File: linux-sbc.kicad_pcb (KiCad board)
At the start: 8 copper layers, 548 parts, among them J1001 7499010121A, J101 Mini-fit Jr 5569, J1101 DM3AT-SF-PEJM5, J1201 PH1-08-UA, J1202 EMI shield frame, J1203 FH12A-40S-0.5SH(55), J1301 SMA RF2-04, J201 61300211121, J202 61300211121, J203 61300211121, J204 61300211121, J205 61300211121, J206 61300211121, J207 61300211121, J208 61300211121, J301 61300211121, J302 61300211121, J303 EMI shield frame, J401 EMI shield frame, J701 USB4105-GF-A, J702 TC2050-NL, J901 AU-Y1008-2-BLK, J902 AU-Y1008-2-BLK, Q201 DMPH4029LFGQ, Q202 DMPH4029LFGQ, Q203 DMN65D8L, Q204 DMPH4029LFGQ, Q205 DMPH4029LFGQ, SW501 JS202011CQN, U1001 LAN8742A-CZ-TR, U1201 TCA9554PW, U1202 AP5725FDCG-7, U1301 LBEE5KL1YN-814, U201 LM4040-5.0, U202 TL331, U203 OPA197, U204 LM4040-5.0, U205 TL331, U206 LM4040-5.0, U207 TL331, U301 AP64500SP-13, U302 AP64500SP-13, U401 STPMIC1DPQR, U501 STM32MP135FAE7, U701 FT231XQ-R, U702 TCA9554PW, U801 MT41K256M16TW, U901 USB2514B/M2, U902 AP22966DC8-7, U903 AP22966DC8-7, Y501 32.768 kHz, Y502 24 MHz, Y901 24 MHz

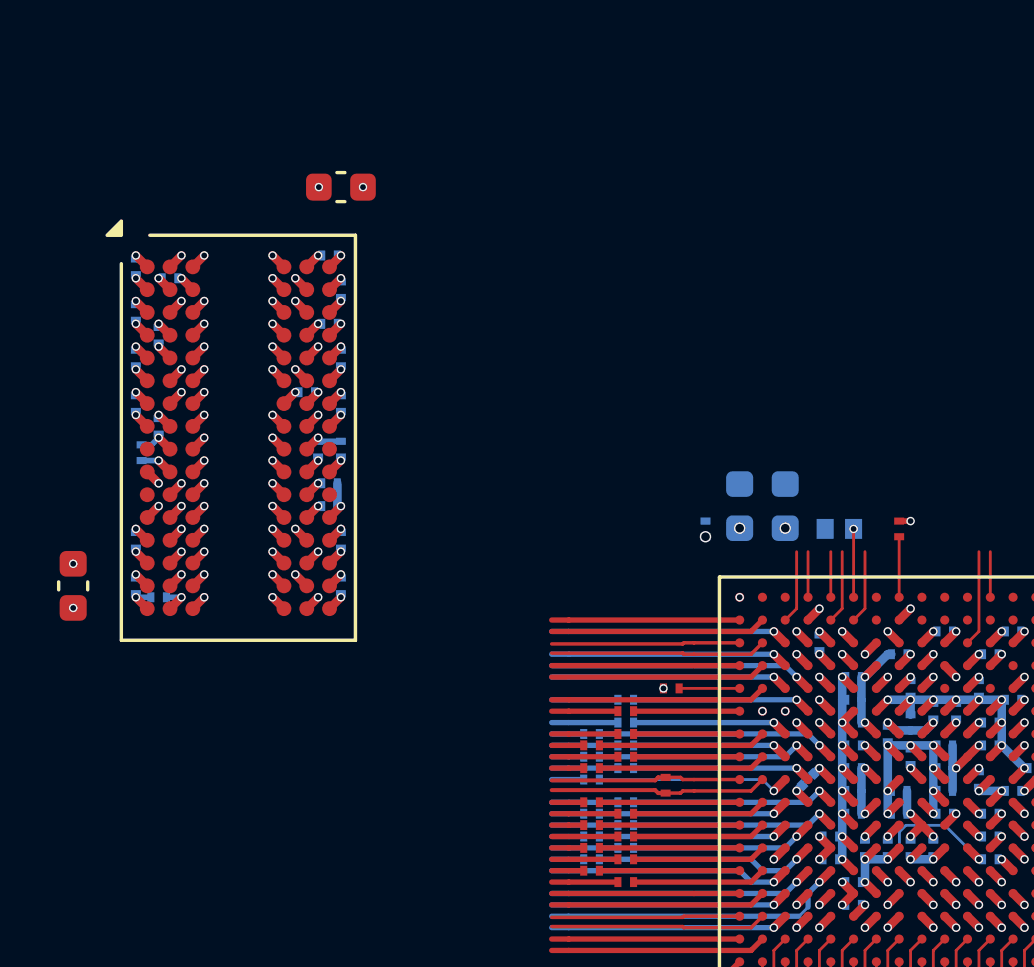
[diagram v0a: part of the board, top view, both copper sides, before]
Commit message: Start layout for DDR power
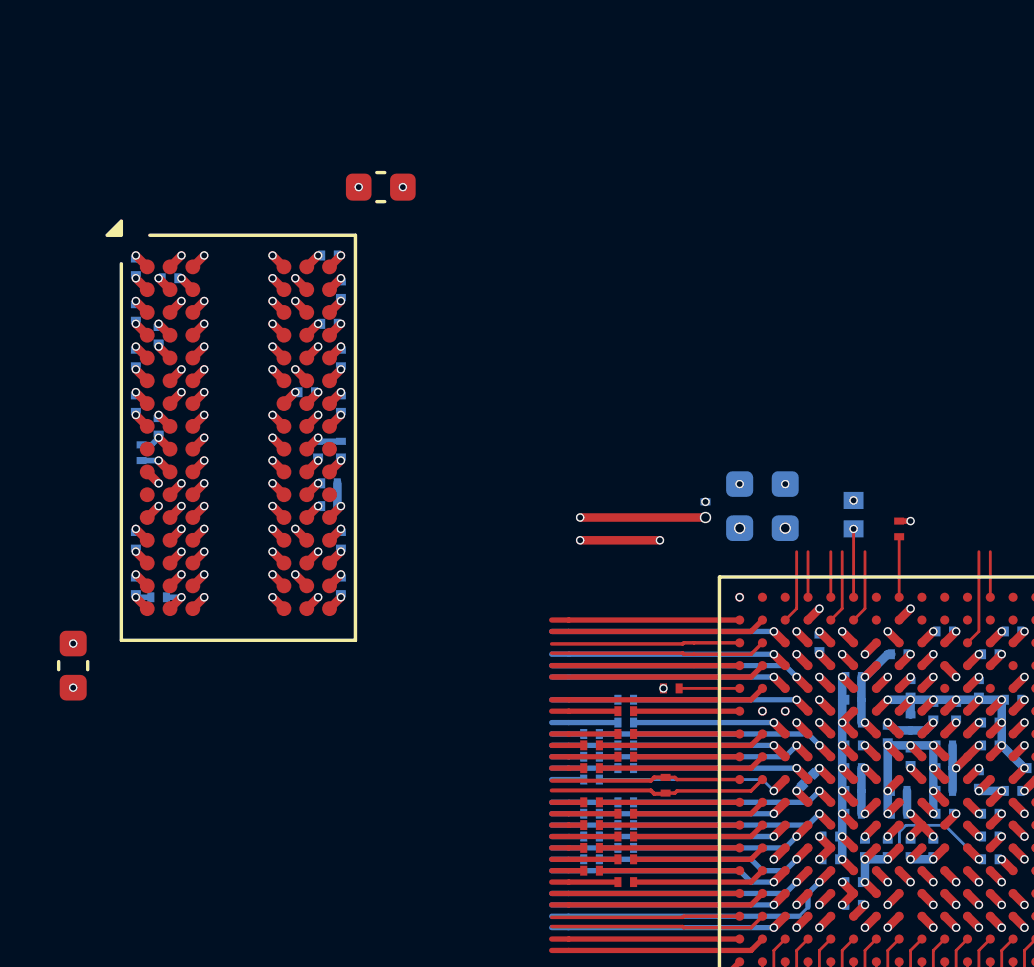
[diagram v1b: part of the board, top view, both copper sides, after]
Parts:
- moved C802 2.80 mm to (-329.8, 96.0)
- moved C801 1.40 mm to (-319.0, 79.2)
- moved R502 0.71 mm to (-302.4, 90.7), turned to 90 degrees
- moved C501 0.67 mm to (-307.6, 90.5)
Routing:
- net /DDR/VDD_DDR: track 32.2 -> 56.2 mm, vias 32 -> 34
- net /DDR/VREF_DDR: track 16.0 -> 39.2 mm, vias 5 -> 6
- net /MPU/VDD_SD_IO: track 27.4 -> 29.8 mm
- net /MPU/VDD_CPU: track 46.7 -> 48.6 mm
- net /MPU/VDD_CORE: track 37.4 -> 39.0 mm
- net GND: vias 243 -> 247
- added copper zone on In2.Cu, net /DDR/VDD_DDR

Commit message: Layout the ethernet section
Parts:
- C1002, C1007, C1008, R1025, R1026: moved to B.Cu
- moved C1007 309.7 mm to (-103.2, -197.0), turned to 90 degrees
- moved C1008 306.1 mm to (-99.6, -191.5), turned to 180 degrees
- moved R1026 301.0 mm to (-96.6, -189.7)
- moved R1025 299.2 mm to (-102.9, -190.2), turned to -90 degrees
- moved R1024 298.7 mm to (-98.0, -184.5), turned to 180 degrees
- moved D1001 298.2 mm to (-100.0, -185.8), turned to 90 degrees
- moved R1023 297.0 mm to (-99.5, -184.5)
- moved R1022 294.7 mm to (-100.5, -183.9), turned to 180 degrees
- moved R1020 291.4 mm to (-102.0, -183.9)
- moved C1006 289.3 mm to (-101.9, -178.0), turned to 180 degrees
- moved R1017 288.8 mm to (-100.5, -173.0)
- moved C1005 288.8 mm to (-96.8, -178.6)
- moved FB1001 288.3 mm to (-96.4, -181.3), turned to 180 degrees
- moved R1021 288.2 mm to (-101.2, -179.0), turned to 180 degrees
- moved R1016 286.0 mm to (-98.5, -171.6)
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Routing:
- net /Ethernet/V_DDA: track 0.00 -> 36.1 mm, vias 0 -> 7
- net CHASSIS: track 0.00 -> 31.7 mm, vias 0 -> 1
- net /Ethernet/LED1_A: track 0.00 -> 26.8 mm, vias 0 -> 2
- net /Ethernet/RX_N: track 0.00 -> 22.1 mm
- net /Ethernet/RX_P: track 0.00 -> 22.1 mm
- net /Ethernet/TX_N: track 0.00 -> 19.0 mm, vias 0 -> 2
- net /Ethernet/TX_P: track 0.00 -> 18.9 mm, vias 0 -> 2
- net /Ethernet/LED2_K: track 0.00 -> 14.2 mm
- net /Ethernet/TXD1: track 0.00 -> 11.1 mm
- net /Ethernet/TXD0: track 0.00 -> 10.0 mm
- net /Ethernet/TXEN: track 0.00 -> 8.80 mm
- net /Ethernet/RST_N: track 0.00 -> 7.32 mm
- net /Ethernet/CLKIN: track 0.00 -> 6.72 mm
- net /Ethernet/MDC: track 0.00 -> 5.24 mm
- net /Ethernet/INT_N: track 0.00 -> 4.38 mm
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- added copper zone on F.Cu, net /Ethernet/V_DDA
- added copper zone on F.Cu, net /Ethernet/V_DDCR

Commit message: Layout the SD card section
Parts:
- C1101: moved to B.Cu
- moved J1101 278.9 mm to (-68.0, -196.0), turned to 180 degrees
- moved C1101 268.3 mm to (-70.2, -183.5), turned to 180 degrees
- moved D1101 264.9 mm to (-68.0, -184.0), turned to -90 degrees
- moved R1109 258.2 mm to (-66.9, -181.0)
- moved R1107 256.5 mm to (-70.0, -182.5)
- moved R1108 255.9 mm to (-66.9, -180.3), turned to 180 degrees
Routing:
- net CHASSIS: track 31.7 -> 75.0 mm, vias 1 -> 6
- net /MPU/uSD.DET_N: track 0.57 -> 31.0 mm, vias 1 -> 4
- net /SD card/D1: track 0.00 -> 11.0 mm
- net /SD card/D2: track 0.00 -> 9.39 mm
- net /PMIC/VDD_SD: track 8.90 -> 18.2 mm, vias 1 -> 2
- net /SD card/CLK: track 0.00 -> 9.12 mm
- net /SD card/CMD: track 0.00 -> 8.85 mm
- net /SD card/D0: track 0.00 -> 8.02 mm, vias 0 -> 1
- net /SD card/D3: track 0.00 -> 6.64 mm, vias 0 -> 1
- net GND: vias 270 -> 274
- net /MPU/VDD_SD_IO: vias 2 -> 3
- net /Debug/VDD: vias 24 -> 25
